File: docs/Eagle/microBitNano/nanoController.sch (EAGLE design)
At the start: 12 parts, among them J2 MTXNRX, J3 IR RX, J4 IR TX, J8 MRXNTX

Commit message: crossover
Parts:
- added J10, J11, J12, J13, J14, J15, J16, J26, J27, J9: (no value), SparkFun-Connectors:CONN_01
- added J17, J18, J19, J20, J21, J22, J23, J24: IR RX, SparkFun-Connectors:CONN_03
- added J25: (no value), SparkFun-Connectors:CONN_11
- added J28: MTXNRX, SparkFun-Connectors:CONN_02
- added LED3: (no value), SparkFun-Connectors:CONN_04LONGPADS
- added R1, R2, R3: (no value), resistor-power:RHPS58
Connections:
- new net 3.3V: J10.1, J28.2, J5.1
- new net 7.4V: J14.1, J15.1, J9.1
- new net D11: JP5.14
- new net D12: JP5.15
- new net N$1: LED3.4, R1.2
- new net N$2: LED3.3, R2.2
- new net N$3: LED3.1, R3.1
- net D2: now also J26.1
- net D4: now also R1.1
- net D7: now also R2.1
- net D8: now also R3.2
- net GND: now also J11.1, J12.1, J13.1, J16.1, J17.1, J18.1, J19.1, J20.1, J21.1, J22.1, J23.1, J24.1, J27.1
- net M0: now also J17.3
- net M1: now also J18.3
- net M10: now also J25.3
- net M11: now also J25.4
- net M12: now also J25.5
- net M13: now also J25.6
- net M14: now also J25.7
- net M15: now also J25.8
- net M16: now also J25.9; no longer JP5.15
- net M19: now also J25.10
- net M2: now also J19.3
- net M20: now also J25.11
- net M3: now also J20.3
- net M4: now also J21.3
- net M5: now also J22.3
- net M6: now also J23.3
- net M7: now also J24.3
- net M8: now also J25.1; no longer JP5.14
- net M9: now also J25.2
- net VCC: now also J17.2, J18.2, J19.2, J20.2, J21.2, J22.2, J23.2, J24.2, J28.1, LED3.2; no longer J5.1
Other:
- note added: "USB"

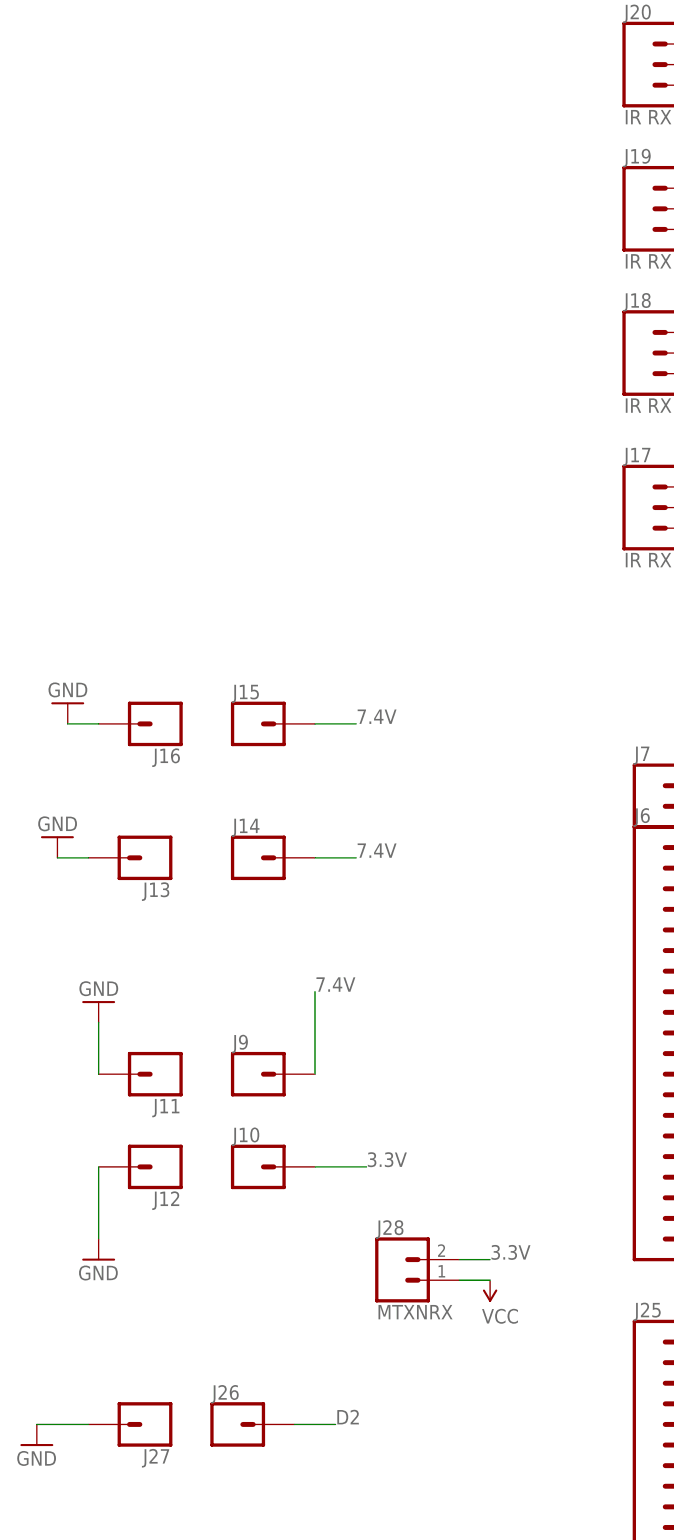
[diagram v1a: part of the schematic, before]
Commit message: Added spider/biped assembly
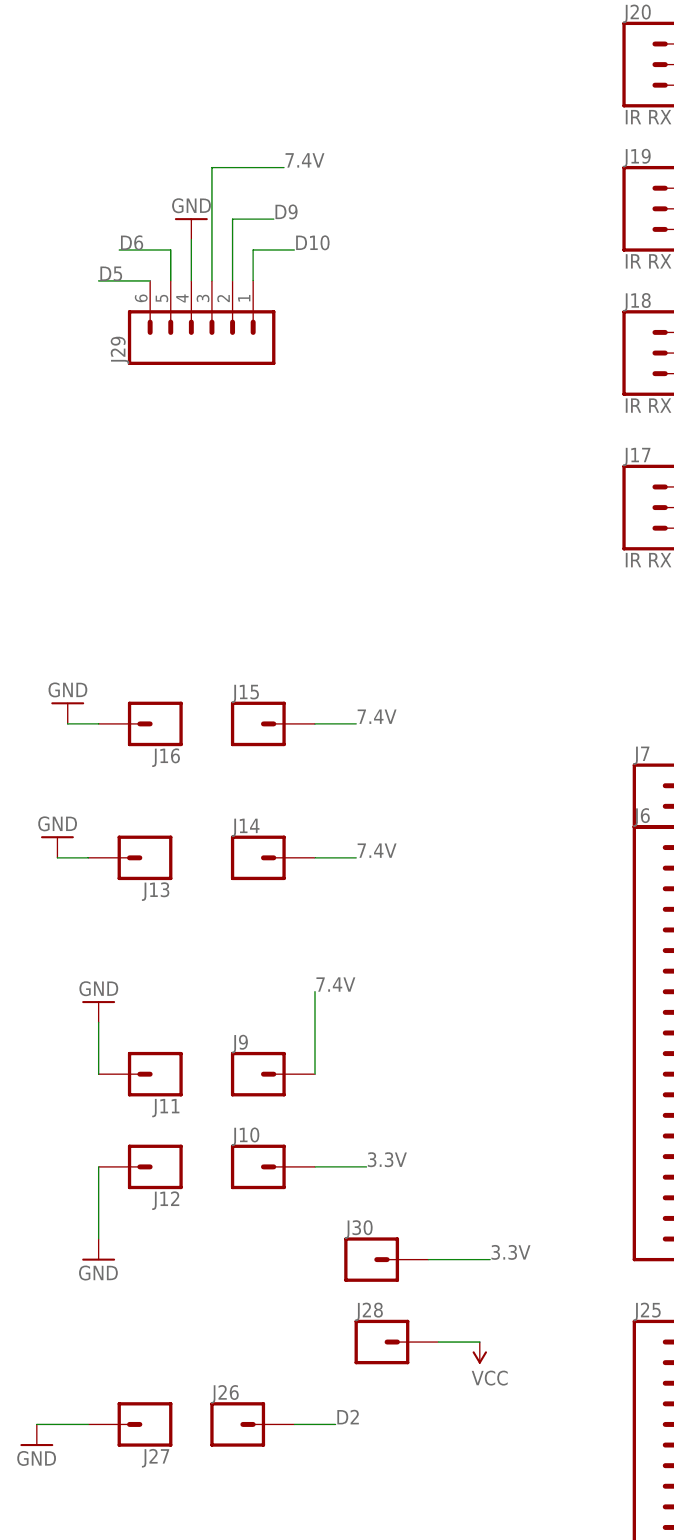
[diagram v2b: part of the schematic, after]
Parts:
- added J29: (no value), SparkFun-Connectors:CONN_06SILK_FEMALE_PTH
- added J30: (no value), SparkFun-Connectors:CONN_01
- J28: value MTXNRX -> (none); device SparkFun-Connectors:CONN_02 -> SparkFun-Connectors:CONN_01
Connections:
- net 3.3V: now also J30.1; no longer J28.2
- net 7.4V: now also J29.3
- net D10: now also J29.1
- net D5: now also J29.6
- net D6: now also J29.5
- net D9: now also J29.2
- net GND: now also J29.4
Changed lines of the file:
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@@
 <part name="R2" library="resistor-power" library_urn="urn:adsk.eagle:library:344" deviceset="R" device="HPS58" package3d_urn="urn:adsk.eagle:package:25160/1"/>
 <part name="R3" library="resistor-power" library_urn="urn:adsk.eagle:library:344" deviceset="R" device="HPS58" package3d_urn="urn:adsk.eagle:package:25160/1"/>
-<part name="J28" library="SparkFun-Connectors" deviceset="CONN_02" device="" value="MTXNRX"/>
+<part name="J29" library="SparkFun-Connectors" deviceset="CONN_06" device="SILK_FEMALE_PTH"/>
+<part name="GND22" library="SparkFun" deviceset="GND" device=""/>
+<part name="J30" library="SparkFun-Connectors" deviceset="CONN_01" device=""/>
+<part name="J28" library="SparkFun-Connectors" deviceset="CONN_01" device=""/>
 </parts>
 <sheets>
@@
 <attribute name="VALUE" x="-27.94" y="167.64" size="1.778" layer="96"/>
 </instance>
-<instance part="P+2" gate="1" x="22.86" y="167.64" smashed="yes" rot="R180">
-<attribute name="VALUE" x="26.416" y="164.084" size="1.778" layer="96" rot="R180"/>
+<instance part="P+2" gate="1" x="21.59" y="160.02" smashed="yes" rot="R180">
+<attribute name="VALUE" x="25.146" y="156.464" size="1.778" layer="96" rot="R180"/>
 </instance>
 <instance part="J13" gate="G$1" x="-19.05" y="219.71" smashed="yes" rot="R180">
@@
 <attribute name="VALUE" x="185.42" y="230.759" size="1.778" layer="96"/>
 </instance>
-<instance part="J28" gate="G$1" x="11.43" y="167.64" smashed="yes">
-<attribute name="VALUE" x="8.89" y="162.814" size="1.778" layer="96" font="vector"/>
-<attribute name="NAME" x="8.89" y="173.228" size="1.778" layer="95" font="vector"/>
+<instance part="J29" gate="G$1" x="-11.43" y="285.75" smashed="yes" rot="R90">
+<attribute name="VALUE" x="-1.524" y="280.67" size="1.778" layer="96" font="vector" rot="R90"/>
+<attribute name="NAME" x="-22.098" y="280.67" size="1.778" layer="95" font="vector" rot="R90"/>
+</instance>
+<instance part="GND22" gate="1" x="-13.97" y="298.45" smashed="yes" rot="R180">
+<attribute name="VALUE" x="-11.43" y="300.99" size="1.778" layer="96" rot="R180"/>
+</instance>
+<instance part="J30" gate="G$1" x="7.62" y="170.18" smashed="yes">
+<attribute name="VALUE" x="5.08" y="165.354" size="1.778" layer="96" font="vector"/>
+<attribute name="NAME" x="5.08" y="173.228" size="1.778" layer="95" font="vector"/>
+</instance>
+<instance part="J28" gate="G$1" x="8.89" y="160.02" smashed="yes">
+<attribute name="VALUE" x="6.35" y="155.194" size="1.778" layer="96" font="vector"/>
+<attribute name="NAME" x="6.35" y="163.068" size="1.778" layer="95" font="vector"/>
 </instance>
 </instances>
@@
 <wire x1="-33.02" y1="149.86" x2="-26.67" y2="149.86" width="0.1524" layer="91"/>
 </segment>
+<segment>
+<pinref part="J29" gate="G$1" pin="4"/>
+<pinref part="GND22" gate="1" pin="GND"/>
+<wire x1="-13.97" y1="295.91" x2="-13.97" y2="290.83" width="0.1524" layer="91"/>
+</segment>
 </net>
 <net name="D3" class="0">
@@
 <label x="177.8" y="200.66" size="1.778" layer="95"/>
 </segment>
+<segment>
+<pinref part="J29" gate="G$1" pin="6"/>
+<wire x1="-19.05" y1="290.83" x2="-25.4" y2="290.83" width="0.1524" layer="91"/>
+<label x="-25.4" y="290.83" size="1.778" layer="95"/>
+</segment>
 </net>
 <net name="D6" class="0">
@@
 <label x="180.34" y="196.85" size="1.778" layer="95"/>
 </segment>
+<segment>
+<pinref part="J29" gate="G$1" pin="5"/>
+<wire x1="-16.51" y1="290.83" x2="-16.51" y2="294.64" width="0.1524" layer="91"/>
+<wire x1="-16.51" y1="294.64" x2="-22.86" y2="294.64" width="0.1524" layer="91"/>
+<label x="-22.86" y="294.64" size="1.778" layer="95"/>
+</segment>
 </net>
 <net name="D7" class="0">
@@
 <label x="182.88" y="200.66" size="1.778" layer="95"/>
 </segment>
+<segment>
+<pinref part="J29" gate="G$1" pin="2"/>
+<wire x1="-8.89" y1="290.83" x2="-8.89" y2="298.45" width="0.1524" layer="91"/>
+<wire x1="-8.89" y1="298.45" x2="-3.81" y2="298.45" width="0.1524" layer="91"/>
+<label x="-3.81" y="298.45" size="1.778" layer="95"/>
+</segment>
 </net>
 <net name="D13" class="0">
@@
 <label x="185.42" y="196.85" size="1.778" layer="95"/>
 </segment>
+<segment>
+<pinref part="J29" gate="G$1" pin="1"/>
+<wire x1="-6.35" y1="290.83" x2="-6.35" y2="294.64" width="0.1524" layer="91"/>
+<wire x1="-6.35" y1="294.64" x2="-1.27" y2="294.64" width="0.1524" layer="91"/>
+<label x="-1.27" y="294.64" size="1.778" layer="95"/>
+</segment>
 </net>
 <net name="VCC" class="0">
@@
 <pinref part="J28" gate="G$1" pin="1"/>
 <pinref part="P+2" gate="1" pin="VCC"/>
-<wire x1="22.86" y1="167.64" x2="19.05" y2="167.64" width="0.1524" layer="91"/>
+<wire x1="21.59" y1="160.02" x2="16.51" y2="160.02" width="0.1524" layer="91"/>
 </segment>
 </net>
@@
 <label x="6.35" y="236.22" size="1.778" layer="95"/>
 </segment>
+<segment>
+<pinref part="J29" gate="G$1" pin="3"/>
+<wire x1="-11.43" y1="290.83" x2="-11.43" y2="304.8" width="0.1524" layer="91"/>
+<wire x1="-11.43" y1="304.8" x2="-2.54" y2="304.8" width="0.1524" layer="91"/>
+<label x="-2.54" y="304.8" size="1.778" layer="95"/>
+</segment>
 </net>
 <net name="N$1" class="0">
@@
 </segment>
 <segment>
-<pinref part="J28" gate="G$1" pin="2"/>
-<wire x1="19.05" y1="170.18" x2="22.86" y2="170.18" width="0.1524" layer="91"/>
+<wire x1="15.24" y1="170.18" x2="22.86" y2="170.18" width="0.1524" layer="91"/>
 <label x="22.86" y="170.18" size="1.778" layer="95"/>
-</segment>
-<segment>
+<pinref part="J30" gate="G$1" pin="1"/>
+</segment>
+<segment>

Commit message: hyo
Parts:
- added PROTECT-MICROBIT: 1N5817-B, diode:1N5817-B
- added S1: (no value), switch-omron:10-XX
- J3: value IR RX -> (none); device SparkFun-Connectors:CONN_03 -> SparkFun-Connectors:CONN_01
- J4: value IR TX -> (none); device SparkFun-Connectors:CONN_02 -> SparkFun-Connectors:CONN_01
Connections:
- new net BATT3.7V: J4.1, J5.1
- new net BATT7.4V: J14.1, J3.1
- new net N$4: JP7.12, PROTECT-MICROBIT.C
- net 3.3V: no longer J5.1
- net 7.4V: no longer J14.1
- net D17: no longer J3.3
- net D3: now also S1.S1; no longer J4.2
- net GND: now also S1.P1; no longer J3.2, J4.1
- net VCC: now also PROTECT-MICROBIT.A; no longer J3.1, JP7.12
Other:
- note added: "Add Diode to protect microbit here...."
- moved on the sheet: J30
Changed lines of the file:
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@@
 <part name="GND5" library="SparkFun" deviceset="GND" device=""/>
 <part name="P+6" library="SparkFun" deviceset="VCC" device=""/>
-<part name="J3" library="SparkFun-Connectors" deviceset="CONN_03" device="" value="IR RX"/>
-<part name="P+7" library="SparkFun" deviceset="VCC" device=""/>
-<part name="GND6" library="SparkFun" deviceset="GND" device=""/>
-<part name="J4" library="SparkFun-Connectors" deviceset="CONN_02" device="" value="IR TX"/>
-<part name="GND7" library="SparkFun" deviceset="GND" device=""/>
 <part name="J1" library="SparkFun-Connectors" deviceset="CONN_01" device="SMTSO-256-ET-0.165DIA"/>
 <part name="GND4" library="SparkFun" deviceset="GND" device=""/>
@@
 <part name="J30" library="SparkFun-Connectors" deviceset="CONN_01" device=""/>
 <part name="J28" library="SparkFun-Connectors" deviceset="CONN_01" device=""/>
+<part name="J4" library="SparkFun-Connectors" deviceset="CONN_01" device=""/>
+<part name="J3" library="SparkFun-Connectors" deviceset="CONN_01" device=""/>
+<part name="PROTECT-MICROBIT" library="diode" library_urn="urn:adsk.eagle:library:210" deviceset="1N581*" device="" package3d_urn="urn:adsk.eagle:package:43421/1" technology="7-B"/>
+<part name="S1" library="switch-omron" library_urn="urn:adsk.eagle:library:377" deviceset="10-XX" device="" package3d_urn="urn:adsk.eagle:package:27496/1"/>
+<part name="GND6" library="SparkFun" deviceset="GND" device=""/>
 </parts>
 <sheets>
@@
 <text x="203.2" y="138.43" size="1.778" layer="91">3V3</text>
 <text x="179.07" y="128.27" size="1.778" layer="91">USB</text>
+<text x="217.17" y="163.83" size="1.778" layer="91">Add Diode to protect microbit here....</text>
 </plain>
 <instances>
@@
 <attribute name="VALUE" x="101.6" y="198.12" size="1.778" layer="96" rot="R270"/>
 </instance>
-<instance part="P+6" gate="1" x="209.55" y="163.83" smashed="yes" rot="R270">
-<attribute name="VALUE" x="213.106" y="164.846" size="1.778" layer="96" rot="R270"/>
-</instance>
-<instance part="J3" gate="J$1" x="106.68" y="256.54" smashed="yes">
-<attribute name="VALUE" x="104.14" y="249.174" size="1.778" layer="96" font="vector"/>
-<attribute name="NAME" x="104.14" y="262.128" size="1.778" layer="95" font="vector"/>
-</instance>
-<instance part="P+7" gate="1" x="114.3" y="242.57" smashed="yes" rot="R180">
-<attribute name="VALUE" x="117.856" y="239.014" size="1.778" layer="96" rot="R180"/>
-</instance>
-<instance part="GND6" gate="1" x="125.73" y="256.54" smashed="yes" rot="R90">
-<attribute name="VALUE" x="128.27" y="254" size="1.778" layer="96" rot="R90"/>
-</instance>
-<instance part="J4" gate="G$1" x="144.78" y="256.54" smashed="yes">
-<attribute name="VALUE" x="142.24" y="251.714" size="1.778" layer="96" font="vector"/>
-<attribute name="NAME" x="142.24" y="262.128" size="1.778" layer="95" font="vector"/>
-</instance>
-<instance part="GND7" gate="1" x="152.4" y="250.19" smashed="yes">
-<attribute name="VALUE" x="149.86" y="247.65" size="1.778" layer="96"/>
+<instance part="P+6" gate="1" x="213.36" y="156.21" smashed="yes" rot="R180">
+<attribute name="VALUE" x="214.376" y="152.654" size="1.778" layer="96" rot="R180"/>
 </instance>
 <instance part="J1" gate="G$1" x="81.28" y="218.44" smashed="yes">
@@
 <attribute name="VALUE" x="-11.43" y="300.99" size="1.778" layer="96" rot="R180"/>
 </instance>
-<instance part="J30" gate="G$1" x="7.62" y="170.18" smashed="yes">
-<attribute name="VALUE" x="5.08" y="165.354" size="1.778" layer="96" font="vector"/>
-<attribute name="NAME" x="5.08" y="173.228" size="1.778" layer="95" font="vector"/>
+<instance part="J30" gate="G$1" x="8.89" y="170.18" smashed="yes">
+<attribute name="VALUE" x="6.35" y="165.354" size="1.778" layer="96" font="vector"/>
+<attribute name="NAME" x="6.35" y="173.228" size="1.778" layer="95" font="vector"/>
 </instance>
 <instance part="J28" gate="G$1" x="8.89" y="160.02" smashed="yes">
 <attribute name="VALUE" x="6.35" y="155.194" size="1.778" layer="96" font="vector"/>
 <attribute name="NAME" x="6.35" y="163.068" size="1.778" layer="95" font="vector"/>
+</instance>
+<instance part="J4" gate="G$1" x="88.9" y="200.66" smashed="yes" rot="R90">
+<attribute name="VALUE" x="93.726" y="198.12" size="1.778" layer="96" font="vector" rot="R90"/>
+<attribute name="NAME" x="85.852" y="198.12" size="1.778" layer="95" font="vector" rot="R90"/>
+</instance>
+<instance part="J3" gate="G$1" x="1.27" y="212.09" smashed="yes" rot="R90">
+<attribute name="VALUE" x="6.096" y="209.55" size="1.778" layer="96" font="vector" rot="R90"/>
+<attribute name="NAME" x="-1.778" y="209.55" size="1.778" layer="95" font="vector" rot="R90"/>
+</instance>
+<instance part="PROTECT-MICROBIT" gate="G$1" x="210.82" y="163.83" smashed="yes" rot="R180">
+<attribute name="NAME" x="242.316" y="163.195" size="1.778" layer="95" rot="R180"/>
+<attribute name="VALUE" x="213.106" y="167.259" size="1.778" layer="96" rot="R180"/>
+</instance>
+<instance part="S1" gate="1" x="226.06" y="227.33" smashed="yes">
+<attribute name="NAME" x="219.71" y="224.79" size="1.778" layer="95" rot="R90"/>
+<attribute name="VALUE" x="222.25" y="230.505" size="1.778" layer="96" rot="R90"/>
+</instance>
+<instance part="GND6" gate="1" x="231.14" y="215.9" smashed="yes" rot="R90">
+<attribute name="VALUE" x="233.68" y="213.36" size="1.778" layer="96" rot="R90"/>
 </instance>
 </instances>
@@
 </segment>
 <segment>
-<pinref part="J3" gate="J$1" pin="2"/>
-<pinref part="GND6" gate="1" pin="GND"/>
-<wire x1="123.19" y1="256.54" x2="114.3" y2="256.54" width="0.1524" layer="91"/>
-</segment>
-<segment>
-<pinref part="J4" gate="G$1" pin="1"/>
-<pinref part="GND7" gate="1" pin="GND"/>
-<wire x1="152.4" y1="252.73" x2="152.4" y2="256.54" width="0.1524" layer="91"/>
-</segment>
-<segment>
 <pinref part="J1" gate="G$1" pin="1"/>
 <pinref part="GND4" gate="1" pin="GND"/>
@@
 <wire x1="-13.97" y1="295.91" x2="-13.97" y2="290.83" width="0.1524" layer="91"/>
 </segment>
+<segment>
+<pinref part="S1" gate="1" pin="P1"/>
+<pinref part="GND6" gate="1" pin="GND"/>
+<wire x1="228.6" y1="215.9" x2="228.6" y2="222.25" width="0.1524" layer="91"/>
+</segment>
 </net>
 <net name="D3" class="0">
@@
 </segment>
 <segment>
-<pinref part="J4" gate="G$1" pin="2"/>
-<wire x1="152.4" y1="259.08" x2="156.21" y2="259.08" width="0.1524" layer="91"/>
-<label x="156.21" y="259.08" size="1.778" layer="95"/>
+<pinref part="S1" gate="1" pin="S1"/>
+<wire x1="228.6" y1="232.41" x2="228.6" y2="240.03" width="0.1524" layer="91"/>
+<wire x1="228.6" y1="240.03" x2="233.68" y2="240.03" width="0.1524" layer="91"/>
+<label x="233.68" y="240.03" size="1.778" layer="95"/>
 </segment>
 </net>
@@
 </segment>
 <segment>
-<pinref part="JP7" gate="G$1" pin="12"/>
-<pinref part="P+6" gate="1" pin="VCC"/>
-<wire x1="209.55" y1="163.83" x2="198.12" y2="163.83" width="0.1524" layer="91"/>
-</segment>
-<segment>
-<pinref part="J3" gate="J$1" pin="1"/>
-<pinref part="P+7" gate="1" pin="VCC"/>
-<wire x1="114.3" y1="242.57" x2="114.3" y2="254" width="0.1524" layer="91"/>
-</segment>
-<segment>
 <pinref part="J6" gate="G$1" pin="20"/>
 <pinref part="P+1" gate="1" pin="VCC"/>
@@
 <wire x1="21.59" y1="160.02" x2="16.51" y2="160.02" width="0.1524" layer="91"/>
 </segment>
+<segment>
+<pinref part="PROTECT-MICROBIT" gate="G$1" pin="A"/>
+<pinref part="P+6" gate="1" pin="VCC"/>
+<wire x1="213.36" y1="156.21" x2="213.36" y2="163.83" width="0.1524" layer="91"/>
+</segment>
 </net>
 <net name="D4" class="0">
@@
 <label x="203.2" y="151.13" size="1.778" layer="95"/>
 </segment>
-<segment>
-<pinref part="J3" gate="J$1" pin="3"/>
-<wire x1="114.3" y1="259.08" x2="118.11" y2="259.08" width="0.1524" layer="91"/>
-<label x="118.11" y="259.08" size="1.778" layer="95"/>
-</segment>
 </net>
 <net name="D18" class="0">
@@
 <wire x1="1.27" y1="193.04" x2="1.27" y2="203.2" width="0.1524" layer="91"/>
 <label x="1.27" y="203.2" size="1.778" layer="95"/>
-</segment>
-<segment>
-<pinref part="J14" gate="G$1" pin="1"/>
-<wire x1="1.27" y1="219.71" x2="6.35" y2="219.71" width="0.1524" layer="91"/>
-<label x="6.35" y="219.71" size="1.778" layer="95"/>
 </segment>
 <segment>
@@
 </segment>
 <segment>
-<wire x1="15.24" y1="170.18" x2="22.86" y2="170.18" width="0.1524" layer="91"/>
+<pinref part="J30" gate="G$1" pin="1"/>
+<wire x1="16.51" y1="170.18" x2="22.86" y2="170.18" width="0.1524" layer="91"/>
 <label x="22.86" y="170.18" size="1.778" layer="95"/>
-<pinref part="J30" gate="G$1" pin="1"/>
-</segment>
+</segment>
+</net>
+<net name="BATT3.7V" class="0">
 <segment>
 <pinref part="J5" gate="G$1" pin="1"/>
-<wire x1="88.9" y1="208.28" x2="91.44" y2="208.28" width="0.1524" layer="91"/>
-<label x="91.44" y="208.28" size="1.778" layer="95"/>
-</segment>
-</net>
+<wire x1="88.9" y1="208.28" x2="92.71" y2="208.28" width="0.1524" layer="91"/>
+<label x="92.71" y="208.28" size="1.778" layer="95"/>
+<pinref part="J4" gate="G$1" pin="1"/>
+<junction x="88.9" y="208.28"/>
+</segment>
+</net>
+<net name="BATT7.4V" class="0">
+<segment>
+<pinref part="J14" gate="G$1" pin="1"/>
+<wire x1="1.27" y1="219.71" x2="12.7" y2="219.71" width="0.1524" layer="91"/>
+<label x="12.7" y="219.71" size="1.778" layer="95"/>
+<pinref part="J3" gate="G$1" pin="1"/>
+<junction x="1.27" y="219.71"/>
+</segment>
+</net>
+<net name="N$4" class="0">
+<segment>
+<pinref part="JP7" gate="G$1" pin="12"/>
+<pinref part="PROTECT-MICROBIT" gate="G$1" pin="C"/>
+<wire x1="208.28" y1="163.83" x2="198.12" y2="163.83" width="0.1524" layer="91"/>
+</segment>
+</net>
